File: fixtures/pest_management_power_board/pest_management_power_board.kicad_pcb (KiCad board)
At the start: 2 copper layers, 100 x 60 mm, 7 parts, among them J2 SEALED_HV_MODULE, J3 HV_POS_GRID, J4 HV_NEG_GRID, SW1 MOMENTARY_5A_DC

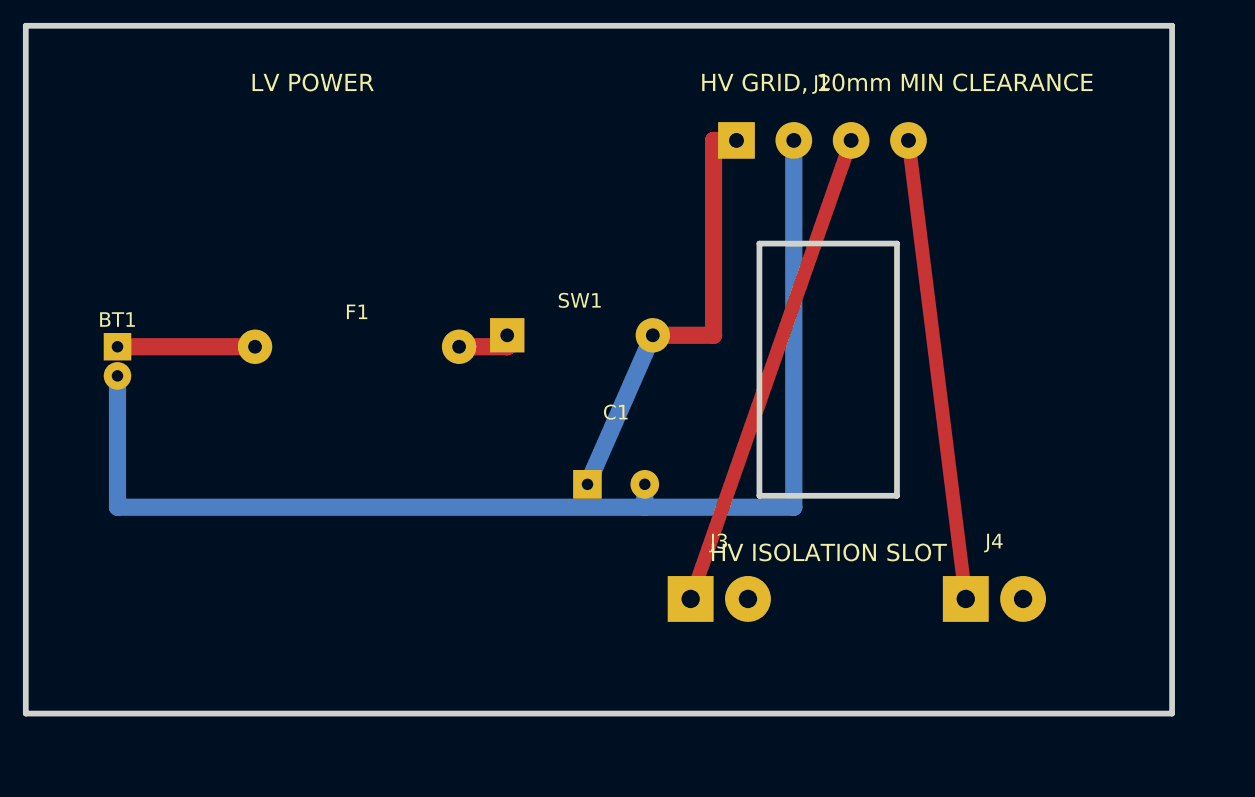
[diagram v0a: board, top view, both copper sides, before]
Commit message: Fix HV clearance geometry and switch interface
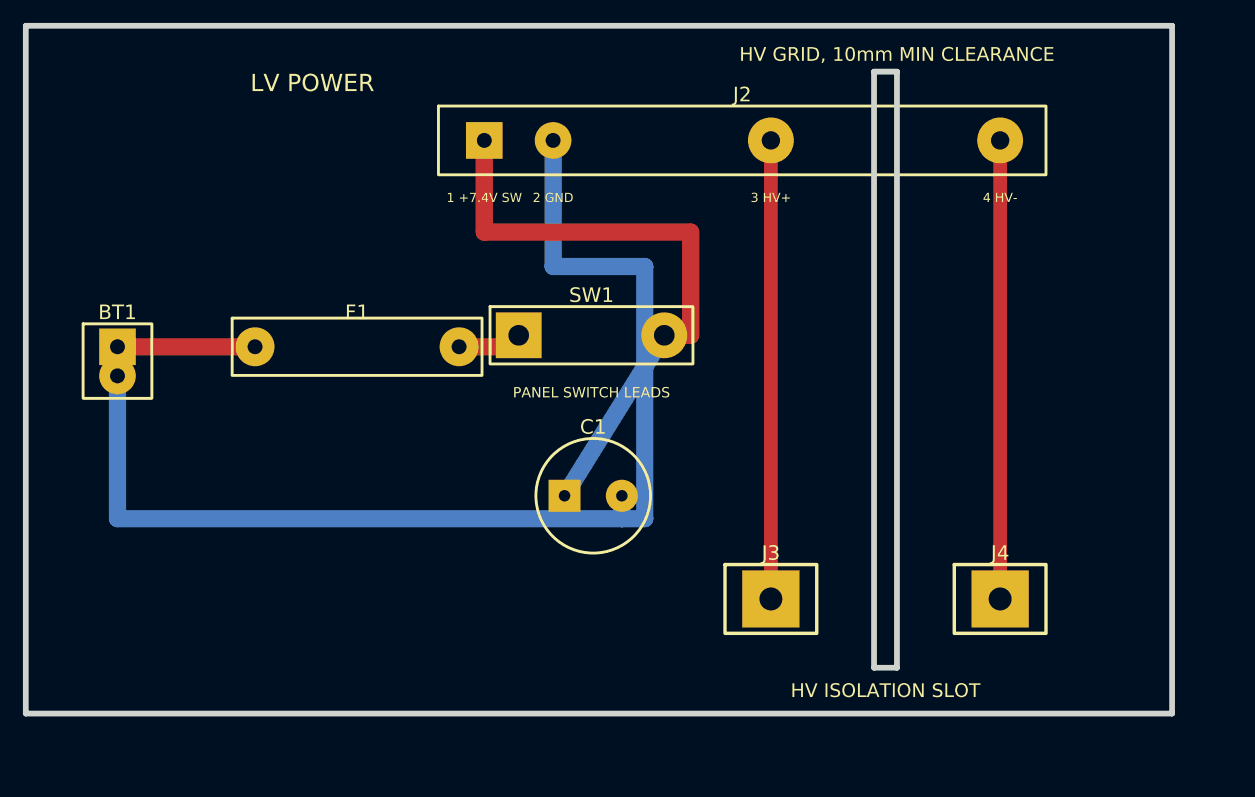
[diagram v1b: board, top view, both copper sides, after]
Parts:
- BT1: footprint Connector_PinHeader_2.54mm:PinHeader_1x02_P2.54mm_Vertical -> Custom:BATTERY_2S_INPUT
- C1: value 470uF 25V -> 470uF_25V; footprint Capacitor_THT:CP_Radial_D10.0mm_P5.00mm -> Custom:CP_RADIAL_10MM_P5
- F1: value 5A_FAST -> 5A_FAST_5x20; footprint Fuse:Fuseholder_Clip-5x20mm_Bel_FC-203-22_Lateral_P17.80x5.00mm_D1.17mm_Horizontal -> Custom:FUSE_5X20_CLIP_17.8MM
- J2: value SEALED_HV_MODULE -> SEALED_COMMERCIAL_HV_MODULE_INTERFACE; footprint TerminalBlock_Phoenix:TerminalBlock_Phoenix_MKDS-1,5-4_1x04_P5.00mm_Horizontal -> Custom:HV_MODULE_4PIN_ISOLATED
- J3, J4: footprint TerminalBlock_Phoenix:TerminalBlock_Phoenix_MKDS-1,5-2_1x02_P5.00mm_Horizontal -> Custom:HV_GRID_SINGLE_SCREW_TERMINAL
- SW1: value MOMENTARY_5A_DC -> MOMENTARY_NO_5A_DC_MIN; footprint Button_Switch_THT:SW_PUSH_6mm -> Custom:PANEL_SWITCH_5A_LEADS
- moved J2 87.3 mm to (0.00, 0.00)
- moved J3 7.00 mm to (85.0, 70.0)
- moved J4 3.00 mm to (105.0, 70.0)
- moved C1 2.24 mm to (67.0, 61.0)
- moved SW1 1.00 mm to (63.0, 47.0)
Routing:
- net +7V4_SW: track 38.5 -> 53.8 mm
- net GND: track 104.5 -> 101.5 mm
- net HV_POS: track 42.4 -> 40.0 mm
- net +7V4_FUSED: track 5.20 -> 6.20 mm
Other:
- outline, holes or cut-outs redrawn
- board text added: "WARNING: HV MODULE/GRID CONNECTIONS"

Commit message: Increase HV to LV separation above 10mm
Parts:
- moved J3 5.00 mm to (90.0, 70.0)
- moved J4 5.00 mm to (110.0, 70.0)
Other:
- outline, holes or cut-outs redrawn
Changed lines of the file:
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@@
   (net 6 "HV_NEG")
   (gr_rect (start 20 20) (end 120 80) (stroke (width 0.5) (type default)) (fill none) (layer "Edge.Cuts"))
-  (gr_rect (start 94 24) (end 96 76) (stroke (width 0.5) (type default)) (fill none) (layer "Edge.Cuts"))
-  (gr_text "HV ISOLATION SLOT" (at 95 78) (layer "F.SilkS") (effects (font (size 1.2 1.2) (thickness 0.25))))
-  (gr_text "HV GRID, 10mm MIN CLEARANCE" (at 96 22.5) (layer "F.SilkS") (effects (font (size 1.2 1.2) (thickness 0.25))))
+  (gr_rect (start 99 24) (end 101 76) (stroke (width 0.5) (type default)) (fill none) (layer "Edge.Cuts"))
+  (gr_text "HV ISOLATION SLOT" (at 100 78) (layer "F.SilkS") (effects (font (size 1.2 1.2) (thickness 0.25))))
+  (gr_text "HV GRID, 10mm MIN CLEARANCE" (at 98 22.5) (layer "F.SilkS") (effects (font (size 1.2 1.2) (thickness 0.25))))
   (gr_text "LV POWER" (at 45 25) (layer "F.SilkS") (effects (font (size 1.5 1.5) (thickness 0.3))))
-  (gr_text "WARNING: HV MODULE/GRID CONNECTIONS" (at 96 25.5) (layer "B.SilkS") (effects (font (size 1.0 1.0) (thickness 0.2))))
+  (gr_text "WARNING: HV MODULE/GRID CONNECTIONS" (at 98 25.5) (layer "B.SilkS") (effects (font (size 1.0 1.0) (thickness 0.2))))
   (footprint "Custom:BATTERY_2S_INPUT" (layer "F.Cu") (at 28 48)
     (property "Reference" "BT1" (at 0 -3 0) (layer "F.SilkS"))
@@
   )
   (footprint "Custom:HV_MODULE_4PIN_ISOLATED" (layer "F.Cu") (at 0 0)
-    (property "Reference" "J2" (at 82.5 26 0) (layer "F.SilkS"))
-    (property "Value" "SEALED_COMMERCIAL_HV_MODULE_INTERFACE" (at 82.5 34 0) (layer "F.Fab") hide)
-    (fp_rect (start 56 27) (end 109 33) (stroke (width 0.25) (type default)) (fill none) (layer "F.SilkS"))
+    (property "Reference" "J2" (at 85 26 0) (layer "F.SilkS"))
+    (property "Value" "SEALED_COMMERCIAL_HV_MODULE_INTERFACE" (at 85 34 0) (layer "F.Fab") hide)
+    (fp_rect (start 56 27) (end 114 33) (stroke (width 0.25) (type default)) (fill none) (layer "F.SilkS"))
     (fp_text user "1 +7.4V SW" (at 60 35 0) (layer "F.SilkS") (effects (font (size 0.8 0.8) (thickness 0.15))))
     (fp_text user "2 GND" (at 66 35 0) (layer "F.SilkS") (effects (font (size 0.8 0.8) (thickness 0.15))))
-    (fp_text user "3 HV+" (at 85 35 0) (layer "F.SilkS") (effects (font (size 0.8 0.8) (thickness 0.15))))
-    (fp_text user "4 HV-" (at 105 35 0) (layer "F.SilkS") (effects (font (size 0.8 0.8) (thickness 0.15))))
+    (fp_text user "3 HV+" (at 90 35 0) (layer "F.SilkS") (effects (font (size 0.8 0.8) (thickness 0.15))))
+    (fp_text user "4 HV-" (at 110 35 0) (layer "F.SilkS") (effects (font (size 0.8 0.8) (thickness 0.15))))
     (pad "1" thru_hole rect (at 60 30) (size 3.2 3.2) (drill 1.3) (layers "*.Cu" "*.Mask") (net 3 "+7V4_SW"))
     (pad "2" thru_hole circle (at 66 30) (size 3.2 3.2) (drill 1.3) (layers "*.Cu" "*.Mask") (net 4 "GND"))
-    (pad "3" thru_hole circle (at 85 30) (size 4.0 4.0) (drill 1.6) (layers "*.Cu" "*.Mask") (net 5 "HV_POS"))
-    (pad "4" thru_hole circle (at 105 30) (size 4.0 4.0) (drill 1.6) (layers "*.Cu" "*.Mask") (net 6 "HV_NEG"))
+    (pad "3" thru_hole circle (at 90 30) (size 4.0 4.0) (drill 1.6) (layers "*.Cu" "*.Mask") (net 5 "HV_POS"))
+    (pad "4" thru_hole circle (at 110 30) (size 4.0 4.0) (drill 1.6) (layers "*.Cu" "*.Mask") (net 6 "HV_NEG"))
   )
-  (footprint "Custom:HV_GRID_SINGLE_SCREW_TERMINAL" (layer "F.Cu") (at 85 70)
+  (footprint "Custom:HV_GRID_SINGLE_SCREW_TERMINAL" (layer "F.Cu") (at 90 70)
     (property "Reference" "J3" (at 0 -4 0) (layer "F.SilkS"))
     (property "Value" "HV_POS_GRID" (at 0 4 0) (layer "F.Fab") hide)
@@
     (pad "1" thru_hole rect (at 0 0) (size 5 5) (drill 2) (layers "*.Cu" "*.Mask") (net 5 "HV_POS"))
   )
-  (footprint "Custom:HV_GRID_SINGLE_SCREW_TERMINAL" (layer "F.Cu") (at 105 70)
+  (footprint "Custom:HV_GRID_SINGLE_SCREW_TERMINAL" (layer "F.Cu") (at 110 70)
     (property "Reference" "J4" (at 0 -4 0) (layer "F.SilkS"))
     (property "Value" "HV_NEG_GRID" (at 0 4 0) (layer "F.Fab") hide)
@@
   (segment (start 74 41) (end 66 41) (width 1.5) (layer "B.Cu") (net 4))
   (segment (start 66 41) (end 66 30) (width 1.5) (layer "B.Cu") (net 4))
-  (segment (start 85 30) (end 85 70) (width 1.2) (layer "F.Cu") (net 5))
-  (segment (start 105 30) (end 105 70) (width 1.2) (layer "F.Cu") (net 6))
+  (segment (start 90 30) (end 90 70) (width 1.2) (layer "F.Cu") (net 5))
+  (segment (start 110 30) (end 110 70) (width 1.2) (layer "F.Cu") (net 6))
 )

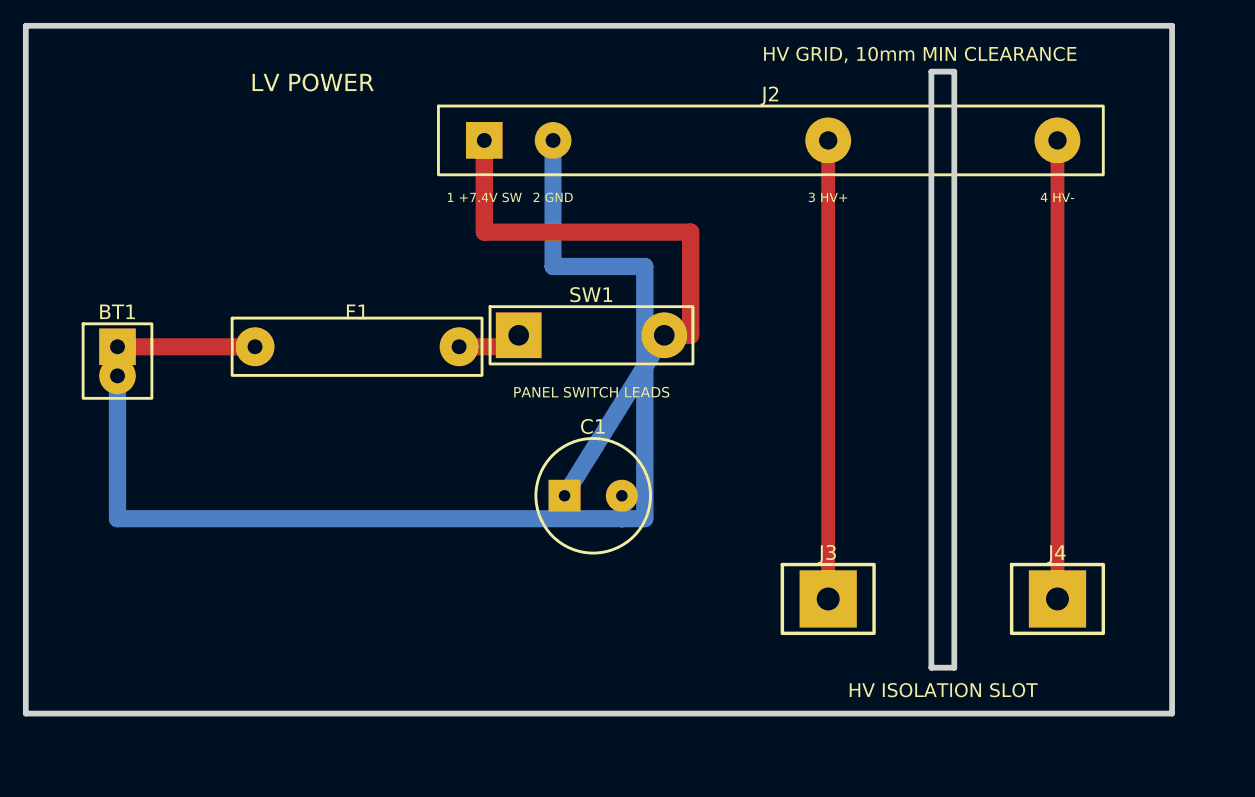
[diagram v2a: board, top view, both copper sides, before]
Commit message: Redesign pest board Rev B for unknown 2S cells and stronger transient delivery
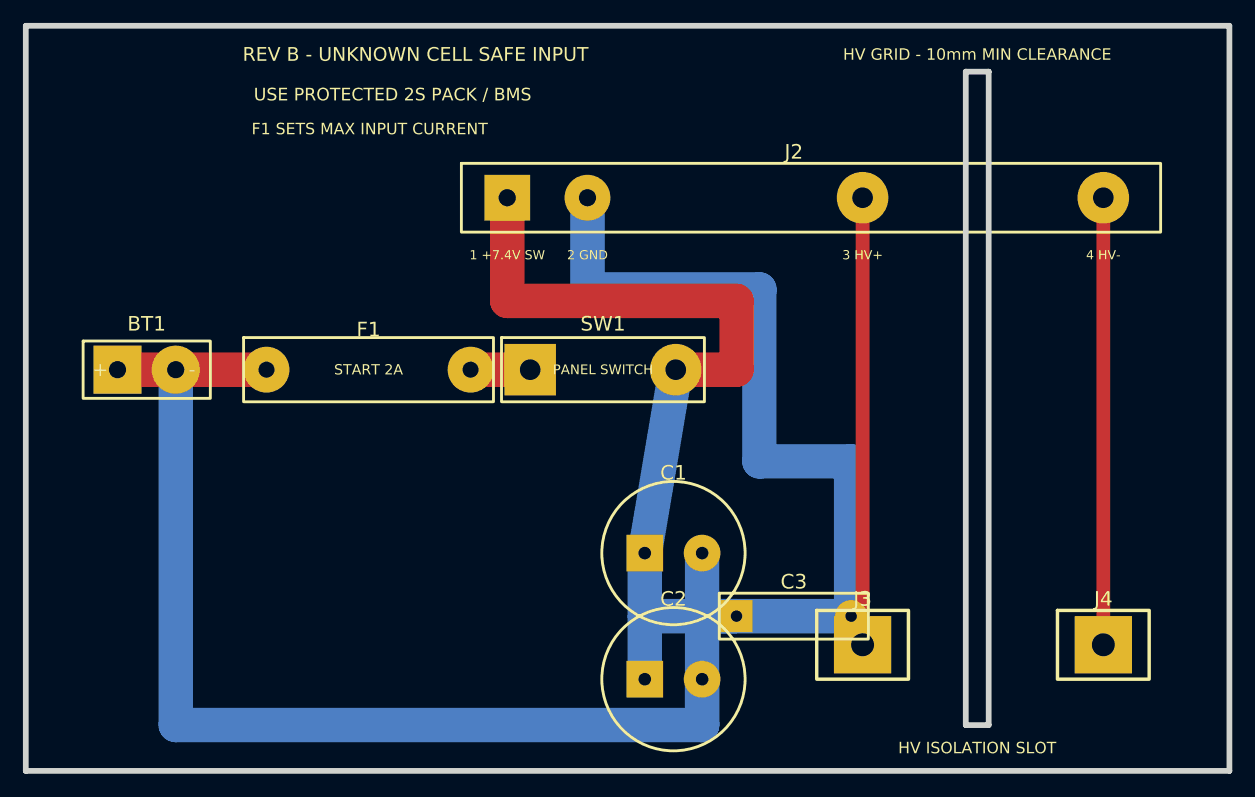
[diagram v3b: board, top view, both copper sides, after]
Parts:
- added C2: 2200uF_16V_LOW_ESR, Custom:CP_RADIAL_12P5MM_P5, F.Cu at (74.0, 77.0)
- added C3: 1uF_25V_FILM, Custom:FILM_CAP_P10, F.Cu at (82.0, 71.5)
- BT1: value 2S_18650_7.4V -> PROTECTED_2S_18650_7.4V; footprint Custom:BATTERY_2S_INPUT -> Custom:BATTERY_2S_INPUT_5P08
- C1: value 470uF_25V -> 2200uF_16V_LOW_ESR; footprint Custom:CP_RADIAL_10MM_P5 -> Custom:CP_RADIAL_12P5MM_P5
- F1: value 5A_FAST_5x20 -> START_2A_FAST_MAX_AFTER_CELL_VALIDATION
- SW1: value MOMENTARY_NO_5A_DC_MIN -> MOMENTARY_NO_10A_DC_PATH; footprint Custom:PANEL_SWITCH_5A_LEADS -> Custom:PANEL_SWITCH_10A_LEADS
- moved C1 8.60 mm to (74.0, 66.0)
- moved J4 5.66 mm to (114.0, 74.0)
- moved J3 5.00 mm to (93.0, 74.0)
- moved SW1 3.16 mm to (64.0, 50.0)
- moved F1 2.24 mm to (41.0, 50.0)
- moved BT1 2.00 mm to (28.0, 50.0)
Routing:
- net GND: track 101.5 -> 168.4 mm
- net +7V4_SW: track 53.8 -> 75.5 mm
- net HV_POS: track 40.0 -> 39.0 mm
- net HV_NEG: track 40.0 -> 39.0 mm
- net +7V4_FUSED: track 6.20 -> 5.20 mm
- net +7V4_BAT: track 12.0 -> 13.0 mm
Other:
- board size 100 x 60 mm -> 105 x 65 mm
- board text added: "F1 SETS MAX INPUT CURRENT"
- board text added: "HV GRID - 10mm MIN CLEARANCE"
- board text added: "REV B - UNKNOWN CELL SAFE INPUT"
- board text added: "USE PROTECTED 2S PACK / BMS"
- board text removed: "HV GRID, 10mm MIN CLEARANCE"
- board text removed: "LV POWER"
- board text removed: "WARNING: HV MODULE/GRID CONNECTIONS"
